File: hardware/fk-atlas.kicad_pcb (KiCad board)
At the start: 2 copper layers, 88.4 x 80.3 mm, 132 parts, among them J1 CONN-HDR-2x5, J2 MICRO-USB, J201 CONN_01X02, J3 Conn_01x02, J301 CONN_01X02, J4 Conn_01x09, J401 CONN_01X02, J501 CONN_01X02, J601 CONN_01X02, M1 MOUNT_HOLE, M2 MOUNT_HOLE, M3 MOUNT_HOLE, M4 MOUNT_HOLE, P2 ATLAS_EC_PROBE, P3 ATLAS_RTD_PROBE, P4 ATLAS_PH_PROBE, P5 ATLAS_DO_PROBE, P6 ATLAS_ORP_PROBE, Q1 2N7002LT1G, Q2 2N7002LT1G, Q3 2N7002LT1G, Q4 2N7002LT1G, Q5 2N7002LT1G, SW1 SPNO, U1 S25FL1xxK0XM, U2 ATSAMD21G18A-AU, U201 ADM3260, U202 ATLAS_EC, U3 MCP1700T-3302E/MB, U301 ADM3260, U302 ATLAS_RTD, U401 ADM3260, U402 ATLAS_PH, U501 ADM3260, U502 ATLAS_DO, U601 ADM3260, U602 ATLAS_ORP, Y1 FC-135

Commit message: Adding fiducials.
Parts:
- added M5: FIDUCIAL, RocketScreamKicadLibrary:FIDUCIAL-1MM, F.Cu at (132.2, 135.4)
- added M6: FIDUCIAL, RocketScreamKicadLibrary:FIDUCIAL-1MM, F.Cu at (126.9, 77.2)
- added M7: FIDUCIAL, RocketScreamKicadLibrary:FIDUCIAL-1MM, F.Cu at (200.9, 65.3)
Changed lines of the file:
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@@
   (general
     (links 353)
-    (no_connects 0)
+    (no_connects 109)
     (area 115.672799 57.328999 204.214801 137.743001)
     (thickness 1.6)
@@
     (tracks 1256)
     (zones 0)
-    (modules 132)
-    (nets 117)
+    (modules 135)
+    (nets 120)
   )
   (page A4)
@@
   (net 115 /PERIPH_GND)
   (net 116 /PERIPH_EN)
+  (net 117 "Net-(M5-Pad~)")
+  (net 118 "Net-(M6-Pad~)")
+  (net 119 "Net-(M7-Pad~)")
   (net_class Default "This is the default net class."
     (clearance 0.1524)
@@
     (add_net "Net-(J501-Pad2)")
     (add_net "Net-(J601-Pad2)")
+    (add_net "Net-(M5-Pad~)")
+    (add_net "Net-(M6-Pad~)")
+    (add_net "Net-(M7-Pad~)")
     (add_net "Net-(Q1-Pad3)")
     (add_net "Net-(Q2-Pad3)")
@@
     (pad "" np_thru_hole circle (at 0 0) (size 2.2 2.2) (drill 2.2) (layers *.Cu *.Mask F.SilkS))
   )
+  (module RocketScreamKicadLibrary:FIDUCIAL-1MM (layer F.Cu)
+    (at 132.1816 135.382)
+    (descr "Circular Fiducial, 1mm bare copper top; 2.54mm keepout")
+    (tags marker)
+    (attr virtual)
+    (fp_text reference M5 (at 0 2.286) (layer F.SilkS) hide
+      (effects (font (size 1 1) (thickness 0.15)))
+    )
+    (fp_text value FIDUCIAL (at 0 -2.032) (layer F.Fab)
+      (effects (font (size 1 1) (thickness 0.15)))
+    )
+    (pad ~ smd circle (at 0 0) (size 1 1) (layers F.Cu F.Mask)
+      (net 117 "Net-(M5-Pad~)") (solder_mask_margin 0.5) (clearance 0.5))
+  )
+  (module RocketScreamKicadLibrary:FIDUCIAL-1MM (layer F.Cu)
+    (at 126.9492 77.216)
+    (descr "Circular Fiducial, 1mm bare copper top; 2.54mm keepout")
+    (tags marker)
+    (attr virtual)
+    (fp_text reference M6 (at 0 2.286) (layer F.SilkS) hide
+      (effects (font (size 1 1) (thickness 0.15)))
+    )
+    (fp_text value FIDUCIAL (at 0 -2.032) (layer F.Fab)
+      (effects (font (size 1 1) (thickness 0.15)))
+    )
+    (pad ~ smd circle (at 0 0) (size 1 1) (layers F.Cu F.Mask)
+      (net 118 "Net-(M6-Pad~)") (solder_mask_margin 0.5) (clearance 0.5))
+  )
+  (module RocketScreamKicadLibrary:FIDUCIAL-1MM (layer F.Cu)
+    (at 200.8632 65.3288)
+    (descr "Circular Fiducial, 1mm bare copper top; 2.54mm keepout")
+    (tags marker)
+    (attr virtual)
+    (fp_text reference M7 (at 0 2.286) (layer F.SilkS) hide
+      (effects (font (size 1 1) (thickness 0.15)))
+    )
+    (fp_text value FIDUCIAL (at 0 -2.032) (layer F.Fab)
+      (effects (font (size 1 1) (thickness 0.15)))
+    )
+    (pad ~ smd circle (at 0 0) (size 1 1) (layers F.Cu F.Mask)
+      (net 119 "Net-(M7-Pad~)") (solder_mask_margin 0.5) (clearance 0.5))
+  )
   (gr_text D13 (at 145.288 104.9528) (layer F.SilkS)

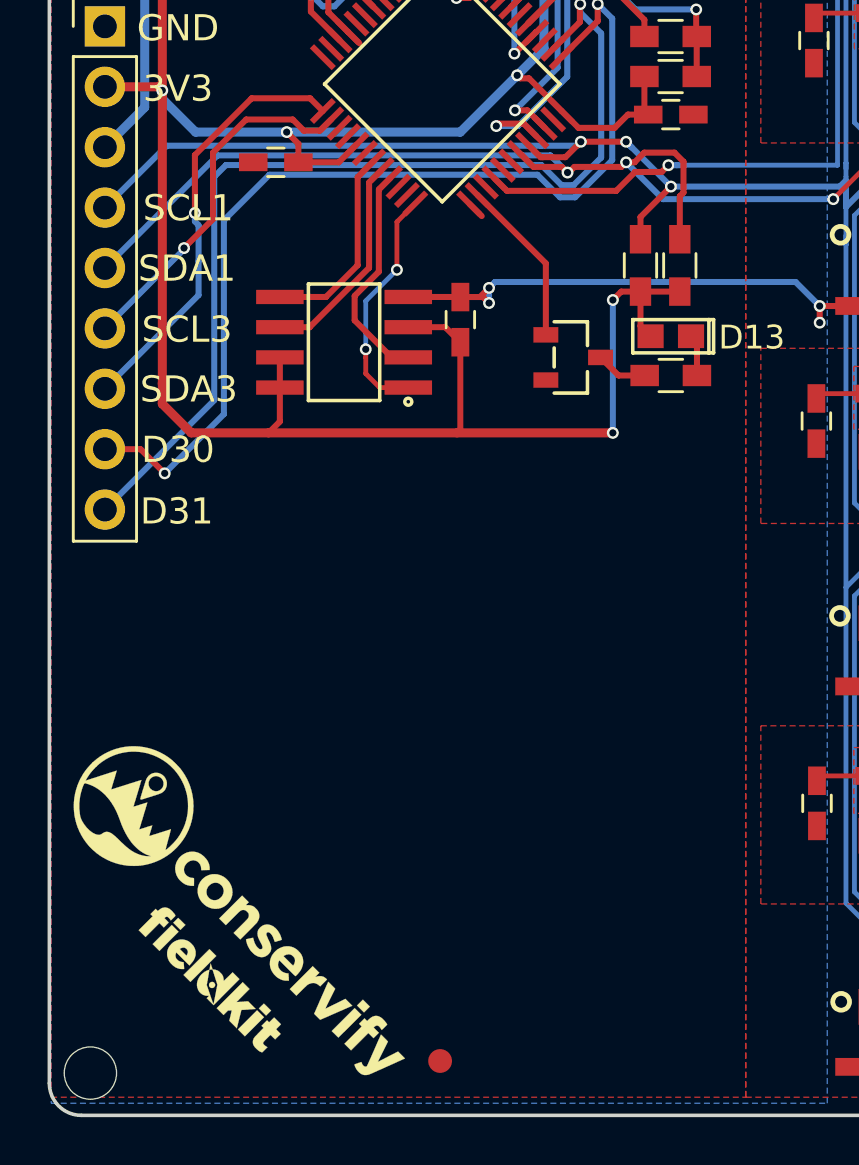
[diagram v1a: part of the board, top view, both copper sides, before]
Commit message: Adding a molex connector.
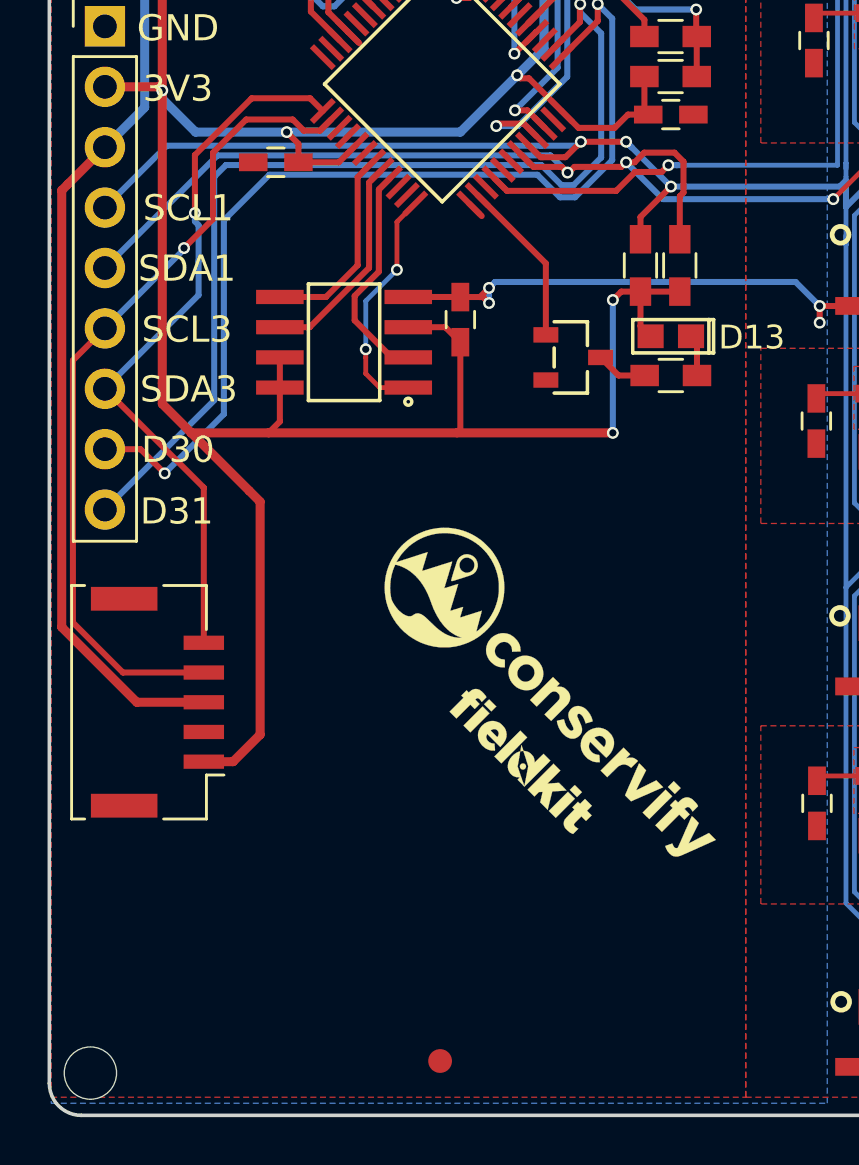
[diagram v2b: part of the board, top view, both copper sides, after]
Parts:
- added J5: Conn_01x05, conservify:Molex_CLIK-Mate_502382-0570_1x05_P1.25mm_Vertical, F.Cu at (120.3, 120.3)
- moved G*** 16.0 mm to (137.0, 120.1)
- moved G*** 16.0 mm to (135.7, 122.7)
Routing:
- net VIN: track 34.2 -> 62.4 mm
- net /SCL3: track 15.2 -> 34.5 mm
- net +3V3: track 336.1 -> 352.8 mm
- net /SDA3: track 18.1 -> 30.5 mm
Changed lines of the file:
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@@
 (kicad_pcb (version 4) (host pcbnew 4.0.7-e2-6376~58~ubuntu16.04.1)
   (general
-    (links 353)
-    (no_connects 109)
+    (links 358)
+    (no_connects 0)
     (area 115.672799 57.328999 204.214801 137.743001)
     (thickness 1.6)
     (drawings 31)
-    (tracks 1256)
+    (tracks 1272)
     (zones 0)
-    (modules 135)
+    (modules 136)
     (nets 120)
   )
@@
   )
   (setup
-    (last_trace_width 0.254)
+    (last_trace_width 0.381)
     (user_trace_width 0.203)
     (user_trace_width 0.381)
@@
   )
   (module conservify:conservify_text_negative_4000 (layer F.Cu)
-    (at 123.9012 129.286 315)
+    (at 136.975061 120.097347 315)
     (fp_text reference G*** (at 0 0 315) (layer F.SilkS) hide
       (effects (font (thickness 0.3)))
@@
   )
   (module conservify:fk_negative_2500 (layer F.Cu)
-    (at 122.5804 131.8768 315)
+    (at 135.654261 122.688147 315)
     (fp_text reference G*** (at 0 0 315) (layer F.SilkS) hide
       (effects (font (thickness 0.3)))
@@
       (net 119 "Net-(M7-Pad~)") (solder_mask_margin 0.5) (clearance 0.5))
   )
+  (module conservify:Molex_CLIK-Mate_502382-0570_1x05_P1.25mm_Vertical (layer F.Cu)
+    (at 120.2944 120.2944 90)
+    (descr "JST CLIK-Mate series connector, 502382-0570 (http://www.molex.com/pdm_docs/sd/5023820270_sd.pdf), generated with kicad-footprint-generator")
+    (tags "connector Molex CLIK-Mate side entry")
+    (attr smd)
+    (fp_text reference J5 (at 0 -4.7 90) (layer F.SilkS) hide
+      (effects (font (size 1 1) (thickness 0.15)))
+    )
+    (fp_text value Conn_01x05 (at 0 4 90) (layer F.Fab)
+      (effects (font (size 1 1) (thickness 0.15)))
+    )
+    (fp_line (start -4.8 1.95) (end 4.8 1.95) (layer F.Fab) (width 0.1))
+    (fp_line (start -4.91 0.26) (end -4.91 2.06) (layer F.SilkS) (width 0.12))
+    (fp_line (start -4.91 2.06) (end -3.06 2.06) (layer F.SilkS) (width 0.12))
+    (fp_line (start -3.06 2.06) (end -3.06 2.8) (layer F.SilkS) (width 0.12))
+    (fp_line (start 4.91 0.26) (end 4.91 2.06) (layer F.SilkS) (width 0.12))
+    (fp_line (start 4.91 2.06) (end 3.06 2.06) (layer F.SilkS) (width 0.12))
+    (fp_line (start -4.91 -3.06) (end -4.91 -3.61) (layer F.SilkS) (width 0.12))
+    (fp_line (start -4.91 -3.61) (end 4.91 -3.61) (layer F.SilkS) (width 0.12))
+    (fp_line (start 4.91 -3.61) (end 4.91 -3.06) (layer F.SilkS) (width 0.12))
+    (fp_line (start -4.8 -3.5) (end 4.8 -3.5) (layer F.Fab) (width 0.1))
+    (fp_line (start -4.8 1.95) (end -4.8 -3.5) (layer F.Fab) (width 0.1))
+    (fp_line (start 4.8 1.95) (end 4.8 -3.5) (layer F.Fab) (width 0.1))
+    (fp_line (start -5.35 -4) (end -5.35 3.3) (layer F.CrtYd) (width 0.05))
+    (fp_line (start -5.35 3.3) (end 5.35 3.3) (layer F.CrtYd) (width 0.05))
+    (fp_line (start 5.35 3.3) (end 5.35 -4) (layer F.CrtYd) (width 0.05))
+    (fp_line (start 5.35 -4) (end -5.35 -4) (layer F.CrtYd) (width 0.05))
+    (fp_line (start -3 1.95) (end -2.5 1.242893) (layer F.Fab) (width 0.1))
+    (fp_line (start -2.5 1.242893) (end -2 1.95) (layer F.Fab) (width 0.1))
+    (fp_text user %R (at 0 -0.77 90) (layer F.Fab)
+      (effects (font (size 1 1) (thickness 0.15)))
+    )
+    (pad 1 smd rect (at -2.5 1.95 90) (size 0.6 1.7) (layers F.Cu F.Paste F.Mask)
+      (net 2 +3V3))
+    (pad 2 smd rect (at -1.25 1.95 90) (size 0.6 1.7) (layers F.Cu F.Paste F.Mask)
+      (net 1 GND))
+    (pad 3 smd rect (at 0 1.95 90) (size 0.6 1.7) (layers F.Cu F.Paste F.Mask)
+      (net 114 VIN))
+    (pad 4 smd rect (at 1.25 1.95 90) (size 0.6 1.7) (layers F.Cu F.Paste F.Mask)
+      (net 110 /SCL3))
+    (pad 5 smd rect (at 2.5 1.95 90) (size 0.6 1.7) (layers F.Cu F.Paste F.Mask)
+      (net 111 /SDA3))
+    (pad "" smd rect (at -4.35 -1.4 90) (size 1 2.8) (layers F.Cu F.Paste F.Mask))
+    (pad "" smd rect (at 4.35 -1.4 90) (size 1 2.8) (layers F.Cu F.Paste F.Mask))
+    (model ${KISYS3DMOD}/Connector_Molex.3dshapes/Molex_CLIK-Mate_502382-0570_1x05_P1.25mm_Vertical.wrl
+      (at (xyz 0 0 0))
+      (scale (xyz 1 1 1))
+      (rotate (xyz 0 0 0))
+    )
+  )
   (gr_text D13 (at 145.288 104.9528) (layer F.SilkS)
     (effects (font (size 1 1) (thickness 0.2)))
@@
   (via (at 135.8392 83.1596) (size 0.5) (drill 0.3) (layers F.Cu B.Cu) (net 1))
   (segment (start 133.513751 82.640249) (end 135.291751 84.418249) (width 0.254) (layer F.Cu) (net 1))
+  (segment (start 124.6124 121.6574) (end 124.6124 111.8616) (width 0.381) (layer F.Cu) (net 2))
+  (segment (start 124.6124 111.8616) (end 124.1552 111.4044) (width 0.381) (layer F.Cu) (net 2))
+  (segment (start 122.2444 122.7944) (end 123.4754 122.7944) (width 0.381) (layer F.Cu) (net 2))
+  (segment (start 123.4754 122.7944) (end 124.6124 121.6574) (width 0.381) (layer F.Cu) (net 2))
+  (segment (start 121.7168 108.966) (end 124.1552 111.4044) (width 0.381) (layer F.Cu) (net 2))
   (segment (start 123.952 81.1276) (end 119.1768 76.3524) (width 0.254) (layer B.Cu) (net 2))
   (segment (start 119.1768 76.3524) (end 119.0244 76.2) (width 0.254) (layer B.Cu) (net 2))
@@
   (via (at 151.384 82.042) (size 0.5) (drill 0.3) (layers F.Cu B.Cu) (net 109))
   (via (at 151.401413 65.913) (size 0.5) (drill 0.3) (layers F.Cu B.Cu) (net 109))
+  (segment (start 118.0846 104.5718) (end 116.7384 105.918) (width 0.254) (layer F.Cu) (net 110))
+  (segment (start 116.7384 105.918) (end 116.7384 116.9416) (width 0.254) (layer F.Cu) (net 110))
+  (segment (start 116.7384 116.9416) (end 118.8412 119.0444) (width 0.254) (layer F.Cu) (net 110))
+  (segment (start 118.8412 119.0444) (end 122.2444 119.0444) (width 0.254) (layer F.Cu) (net 110))
   (segment (start 121.412 101.1936) (end 122.6312 99.9744) (width 0.254) (layer F.Cu) (net 110))
   (segment (start 122.6312 99.9744) (end 122.6312 97.1804) (width 0.254) (layer F.Cu) (net 110))
@@
   (segment (start 125.984113 95.787399) (end 124.024201 95.787399) (width 0.254) (layer F.Cu) (net 110))
   (segment (start 124.024201 95.787399) (end 122.6312 97.1804) (width 0.254) (layer F.Cu) (net 110))
+  (segment (start 122.2444 117.7944) (end 122.2444 111.2716) (width 0.254) (layer F.Cu) (net 111))
+  (segment (start 122.2444 111.2716) (end 118.0846 107.1118) (width 0.254) (layer F.Cu) (net 111))
   (segment (start 122.0216 100.226353) (end 122.0216 101.7524) (width 0.254) (layer B.Cu) (net 111))
   (segment (start 118.0846 107.1118) (end 122.0216 103.1748) (width 0.254) (layer B.Cu) (net 111))
@@
   (segment (start 140.8811 78.1763) (end 140.8811 77.0763) (width 0.381) (layer F.Cu) (net 113))
   (segment (start 140.6931 72.9615) (end 140.7439 72.9107) (width 0.381) (layer F.Cu) (net 113))
+  (segment (start 122.2444 120.2944) (end 119.426647 120.2944) (width 0.381) (layer F.Cu) (net 114))
+  (segment (start 116.26849 98.76791) (end 116.5352 98.5012) (width 0.381) (layer F.Cu) (net 114))
+  (segment (start 119.426647 120.2944) (end 116.26849 117.136243) (width 0.381) (layer F.Cu) (net 114))
+  (segment (start 116.26849 117.136243) (end 116.26849 98.76791) (width 0.381) (layer F.Cu) (net 114))
+  (segment (start 116.5352 98.5012) (end 118.0846 96.9518) (width 0.381) (layer F.Cu) (net 114))
   (segment (start 124.968 83.3628) (end 128.1094 83.3628) (width 0.381) (layer F.Cu) (net 114))
   (segment (start 128.1094 83.3628) (end 130.2938 81.1784) (width 0.381) (layer F.Cu) (net 114))

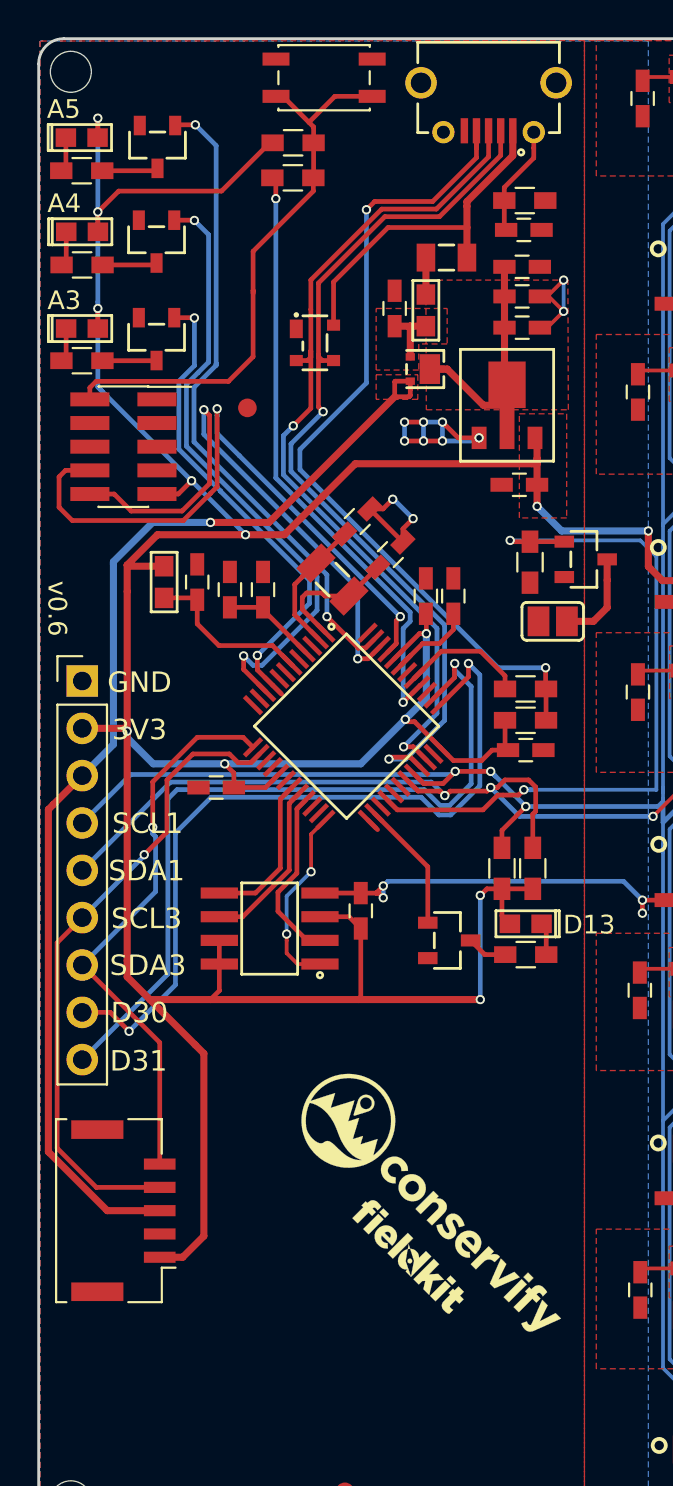
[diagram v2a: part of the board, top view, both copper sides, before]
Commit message: Silkscreen tweaks.
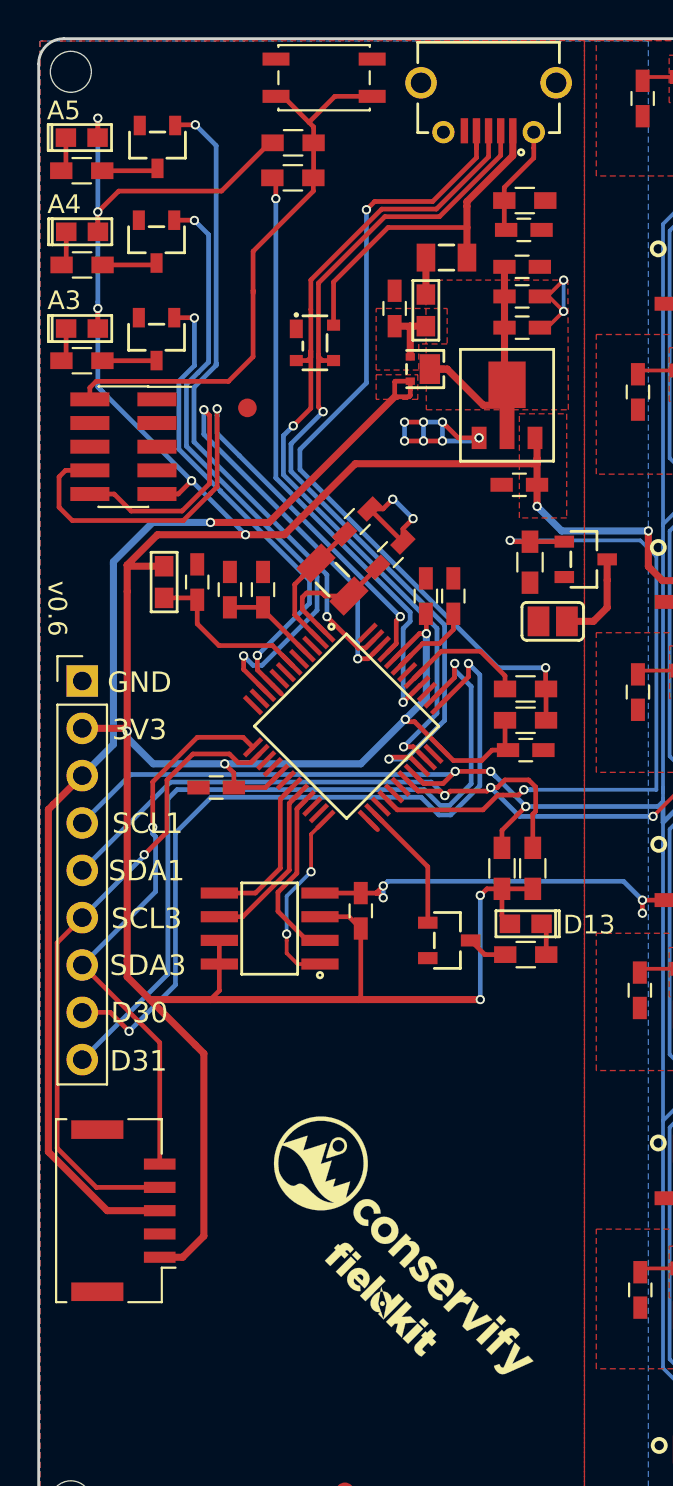
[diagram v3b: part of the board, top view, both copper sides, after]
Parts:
- moved G*** 2.72 mm to (135.5, 122.4)
- moved G*** 2.72 mm to (134.2, 125.0)
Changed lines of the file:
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@@
     (links 358)
     (no_connects 0)
-    (area 115.672799 57.328999 204.214801 137.743001)
+    (area 112.513076 55.0796 223.731401 140.0924)
     (thickness 1.6)
     (drawings 31)
@@
   )
   (setup
-    (last_trace_width 0.381)
+    (last_trace_width 0.254)
     (user_trace_width 0.203)
     (user_trace_width 0.381)
@@
   )
   (module conservify:conservify_text_negative_4000 (layer F.Cu)
-    (at 136.975061 120.097347 315)
+    (at 135.501861 122.383347 315)
     (fp_text reference G*** (at 0 0 315) (layer F.SilkS) hide
       (effects (font (thickness 0.3)))
@@
   )
   (module conservify:fk_negative_2500 (layer F.Cu)
-    (at 135.654261 122.688147 315)
+    (at 134.181061 124.974147 315)
     (fp_text reference G*** (at 0 0 315) (layer F.SilkS) hide
       (effects (font (thickness 0.3)))
@@
     (effects (font (size 1 1) (thickness 0.2)))
   )
-  (gr_text A5 (at 117.094 61.1886) (layer F.SilkS)
+  (gr_text A5 (at 117.094 61.2648) (layer F.SilkS)
     (effects (font (size 1 1) (thickness 0.2)))
   )
-  (gr_text A4 (at 117.1194 66.2432) (layer F.SilkS)
+  (gr_text A4 (at 117.1194 66.294) (layer F.SilkS)
     (effects (font (size 1 1) (thickness 0.2)))
   )

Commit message: Adjust pad mask clearance to avoid exposing ground plane.
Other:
- rule pad_to_mask_clearance: 0.2 -> 0.1
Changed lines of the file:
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@@
     (pad_size 0.25 1.3)
     (pad_drill 0)
-    (pad_to_mask_clearance 0.2)
+    (pad_to_mask_clearance 0.1)
     (aux_axis_origin 0 0)
     (visible_elements 7FFFFF7F)
